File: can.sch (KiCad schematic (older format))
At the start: 6 parts, among them U5 TCAN334

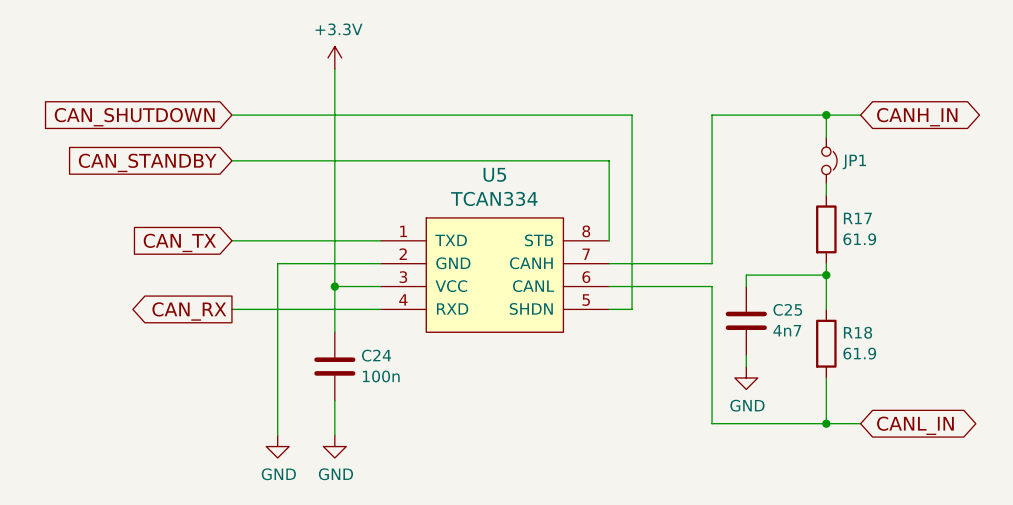
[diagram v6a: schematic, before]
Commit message: 24 V input protection
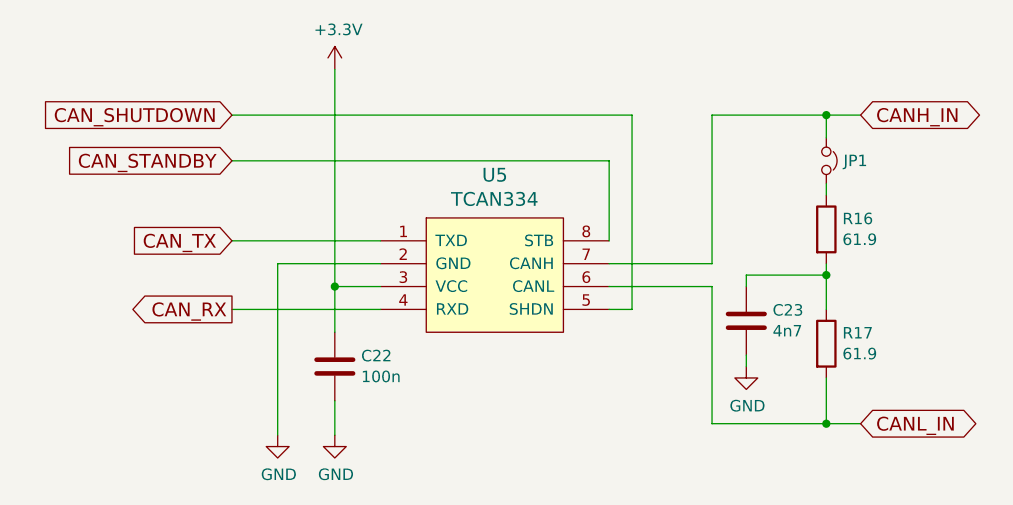
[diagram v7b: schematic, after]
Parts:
- renumbered C24 to C22, C25 to C23, R17 to R16, R18 to R17
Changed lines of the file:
@@
 CANL_IN
 $Comp
-L R R17
+L R R16
 U 1 1 57AEEDFE
 P 6250 3650
-F 0 "R17" H 6320 3696 50  0000 L CNN
+F 0 "R16" H 6320 3696 50  0000 L CNN
 F 1 "61.9" H 6320 3605 50  0000 L CNN
 F 2 "Resistors_SMD:R_0603" V 6180 3650 50  0001 C CNN
@@
 $EndComp
 $Comp
-L R R18
+L R R17
 U 1 1 57AEEEAC
 P 6250 4150
-F 0 "R18" H 6320 4196 50  0000 L CNN
+F 0 "R17" H 6320 4196 50  0000 L CNN
 F 1 "61.9" H 6320 4105 50  0000 L CNN
 F 2 "Resistors_SMD:R_0603" V 6180 4150 50  0001 C CNN
@@
 Connection ~ 6250 3150
 $Comp
-L C C25
+L C C23
 U 1 1 57AEEFE7
 P 5900 4050
-F 0 "C25" H 6015 4096 50  0000 L CNN
+F 0 "C23" H 6015 4096 50  0000 L CNN
 F 1 "4n7" H 6015 4005 50  0000 L CNN
 F 2 "Capacitors_SMD:C_0603" H 5938 3900 50  0001 C CNN
@@
 CAN_STANDBY
 $Comp
-L C C24
+L C C22
 U 1 1 57AF5ACF
 P 4100 4250
-F 0 "C24" H 4215 4296 50  0000 L CNN
+F 0 "C22" H 4215 4296 50  0000 L CNN
 F 1 "100n" H 4215 4205 50  0000 L CNN
 F 2 "Capacitors_SMD:C_0603" H 4138 4100 50  0001 C CNN

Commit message: Add bom, minor changes
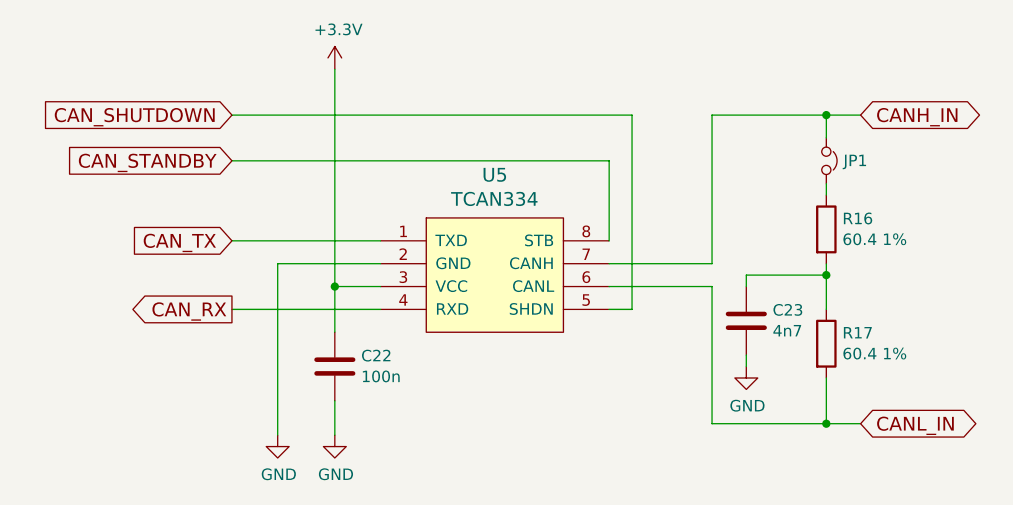
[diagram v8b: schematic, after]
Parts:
- C22, C23: footprint Capacitors_SMD:C_0603 -> (none)
- R16, R17: value 61.9 -> 60.4 1%
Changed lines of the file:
@@
 P 6250 3650
 F 0 "R16" H 6320 3696 50  0000 L CNN
-F 1 "61.9" H 6320 3605 50  0000 L CNN
+F 1 "60.4 1%" H 6320 3605 50  0000 L CNN
 F 2 "Resistors_SMD:R_0603" V 6180 3650 50  0001 C CNN
 F 3 "" H 6250 3650 50  0000 C CNN
@@
 P 6250 4150
 F 0 "R17" H 6320 4196 50  0000 L CNN
-F 1 "61.9" H 6320 4105 50  0000 L CNN
+F 1 "60.4 1%" H 6320 4105 50  0000 L CNN
 F 2 "Resistors_SMD:R_0603" V 6180 4150 50  0001 C CNN
 F 3 "" H 6250 4150 50  0000 C CNN
@@
 F 0 "C23" H 6015 4096 50  0000 L CNN
 F 1 "4n7" H 6015 4005 50  0000 L CNN
-F 2 "Capacitors_SMD:C_0603" H 5938 3900 50  0001 C CNN
+F 2 "" H 5938 3900 50  0001 C CNN
 F 3 "" H 5900 4050 50  0000 C CNN
 	1    5900 4050
@@
 F 0 "C22" H 4215 4296 50  0000 L CNN
 F 1 "100n" H 4215 4205 50  0000 L CNN
-F 2 "Capacitors_SMD:C_0603" H 4138 4100 50  0001 C CNN
+F 2 "" H 4138 4100 50  0001 C CNN
 F 3 "" H 4100 4250 50  0000 C CNN
 	1    4100 4250
